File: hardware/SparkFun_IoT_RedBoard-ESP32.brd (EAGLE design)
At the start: 68.6 x 58.4 mm, 215 parts, among them J1 5.5x2.1mm Barrel, J13 QWIIC_RIGHT_ANGLE, J15 MICRO-SD-PUSH-PUSH-EXT-PIN, J2 USB C, J3 USB_SOLDER_PADS, J5 M10NO_SILK, Q1 MBT3904DW1T1, Q11 20V/4.2A/52mΩ/1.4W, Q13 20V/4.2A/52mΩ/1.4W, Q3 20V/4.2A/52mΩ/1.4W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

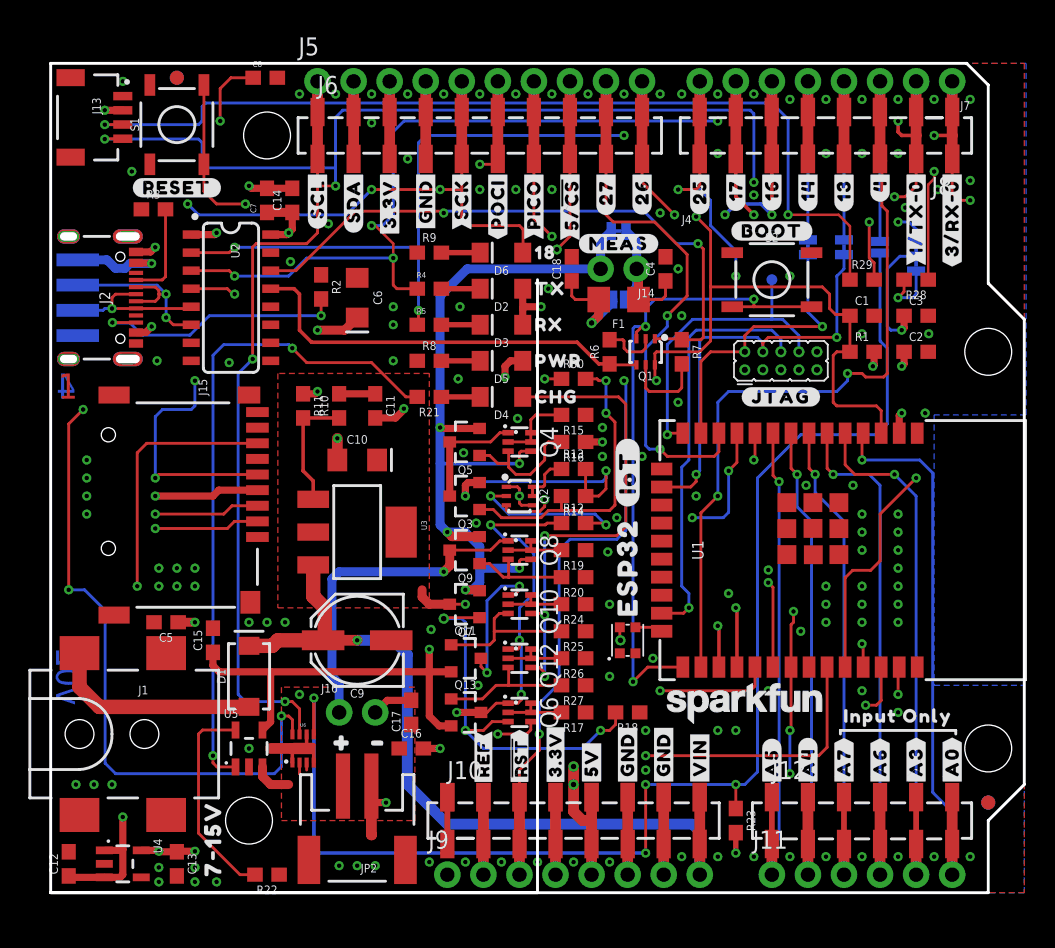
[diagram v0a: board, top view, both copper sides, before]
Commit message: Design review updates
Rename files to remove "v01"
Update libraries
Adjust traces under SD card for keepout region
Change ESP32 footprint from narrow to standard
Change USB-C connector to 4-layer version
Add USB shield jumper
Move CC resistor positions
Adjust parts to be on grid where possible
Move Qwiic logo to top silk (also adjust Reset silk to avoid confusion)
Adjust layer numbers in copper to not overlap
Remove C14
Increase current rating of D1
Add silk to addressable LED
Remove extraneous mill lines
Remove Made in USA silk
Replace MEAS header and jumper with combo jumper
Add fuse value to schematic
Remove voltage ratings from capacitors in schematic
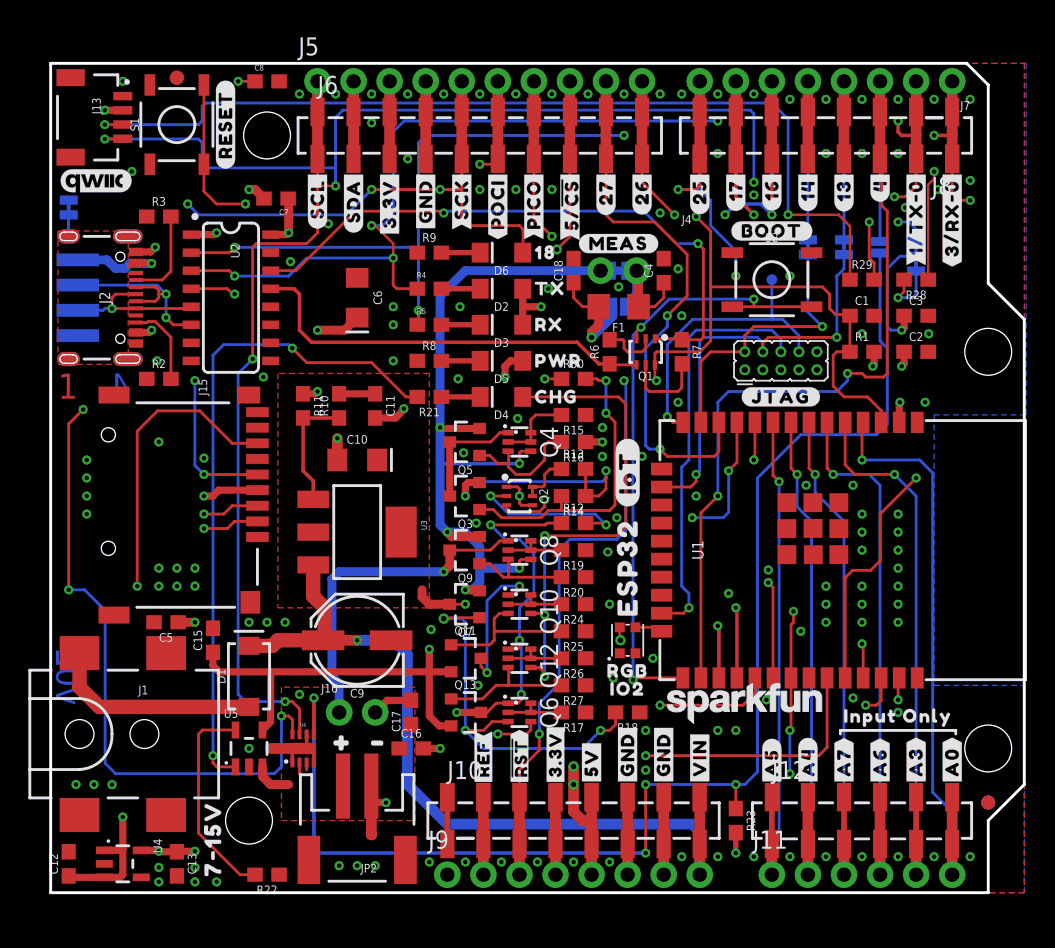
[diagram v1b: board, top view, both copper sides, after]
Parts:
- removed C14: 10uF, SparkFun-Capacitors:0603
- removed J14: (no value), SparkFun-Connectors:1X02_NO_SILK
- removed U$94: (no value), output-ESP32:MADE_IN32321857
- removed U$99: (no value), output-ESP32:THE_USA32321858
- added JP15: SHLD, SparkFun-Jumpers:SMT-JUMPER_2_NC_TRACE_SILK
- added U$65: (no value), output:RGB0
- added U$81: (no value), output:#SHLD#0
- added U$82: (no value), output:IO20
- D1: value 1A/40V/500mV -> 3A/40V/500mV
- F1: value 6V/0.75A -> 6V/0.75A/1.5A
- J2: value USB C -> USB-C; device SparkFun-Connectors:USB-C-16P-2LAYER-PADS -> SparkFun-Connectors:USB-C-16P-4LAYER-ISOLATED
- JP10: value JUMPER-SMT_2_NC_TRACE_SILK -> JUMPER-COMBO_2_NC_TRACE; device SparkFun-Jumpers:SMT-JUMPER_2_NC_TRACE_SILK -> SparkFun-Jumpers:COMBO-JUMPER_2_NC_TRACE
- U$11: device output:#MEAS#0 -> output-ESP32:#MEAS#1851
- U1: value ESP-WROOM-3232D-NARROW -> ESP-WROOM-3232D; device SparkFun-RF:ESP-WROOM-32D-NARROW -> SparkFun-RF:ESP-WROOM-32D
- moved R2 13.1 mm to (7.62, 36.2), turned to 0 degrees
- moved U$11 6.41 mm to (40.0, 45.7)
- moved U$26 5.61 mm to (12.3, 54.1), turned to 90 degrees
- moved LOGO2 4.74 mm to (3.17, 50.2), flipped to the top, turned to 0 degrees
- moved JP10 2.79 mm to (40.0, 43.8)
- moved C7 0.65 mm to (15.9, 48.9), turned to 180 degrees
- moved R3 0.64 mm to (7.62, 47.6)
- moved BYP 0.51 mm to (40.0, 41.3)
- moved F1 0.51 mm to (40.0, 41.3)
- moved U$64 0.51 mm to (45.1, 41.3)
- moved C8 0.28 mm to (15.2, 57.1)
- moved C4 0.18 mm to (43.2, 43.8)
- moved C18 0.18 mm to (36.8, 43.8)
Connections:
- new net SHLD: J2.SHLD1, J2.SHLD2, J2.SHLD3, J2.SHLD4, J2.SHLD5, J2.SHLD6, J2.SHLD7, J2.SHLD8, JP15.2
- net 3.3V: no longer C14.1
- net 5V_MEAS: now also JP10.3; no longer J14.2
- net GND: now also JP15.1, U1.GND; no longer C14.2, U1.GND1
- net N$19: now also JP10.4; no longer J14.1
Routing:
- net CC2: track 18.5 -> 5.88 mm, vias 2 -> 0
- net ESP32_GPIO5_!CS!: track 111.4 -> 104.1 mm
- net ESP32_GPIO23_PICO: track 122.6 -> 115.5 mm
- net ESP32_GPIO18_SCK: track 122.5 -> 117.3 mm
- net 3.3V: track 54.2 -> 49.8 mm
- net 5V_MEAS: track 71.1 -> 68.1 mm
- net ESP32_GPIO19_POCI: track 147.5 -> 150.3 mm
- net V_USB: track 118.5 -> 116.0 mm
- net N$19: track 10.8 -> 8.58 mm
- net ESP32_0: track 46.3 -> 44.5 mm
- net GND: track 46.6 -> 44.8 mm, vias 145 -> 148
- net SHLD: track 0.00 -> 1.52 mm
- net ESP32_EN: track 124.2 -> 122.7 mm
- net N$6: track 21.6 -> 20.4 mm
- net ESP32_GPIO12_TDI: track 21.9 -> 20.8 mm
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- added copper zone on layer 1, net SHLD
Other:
- outline, holes or cut-outs redrawn

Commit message: More design review updates
Add center positive silk marker to barrel jack
Fix air wire errors in ULP by connecting with traces
Add SD card detection with NO jumper to GPIO16
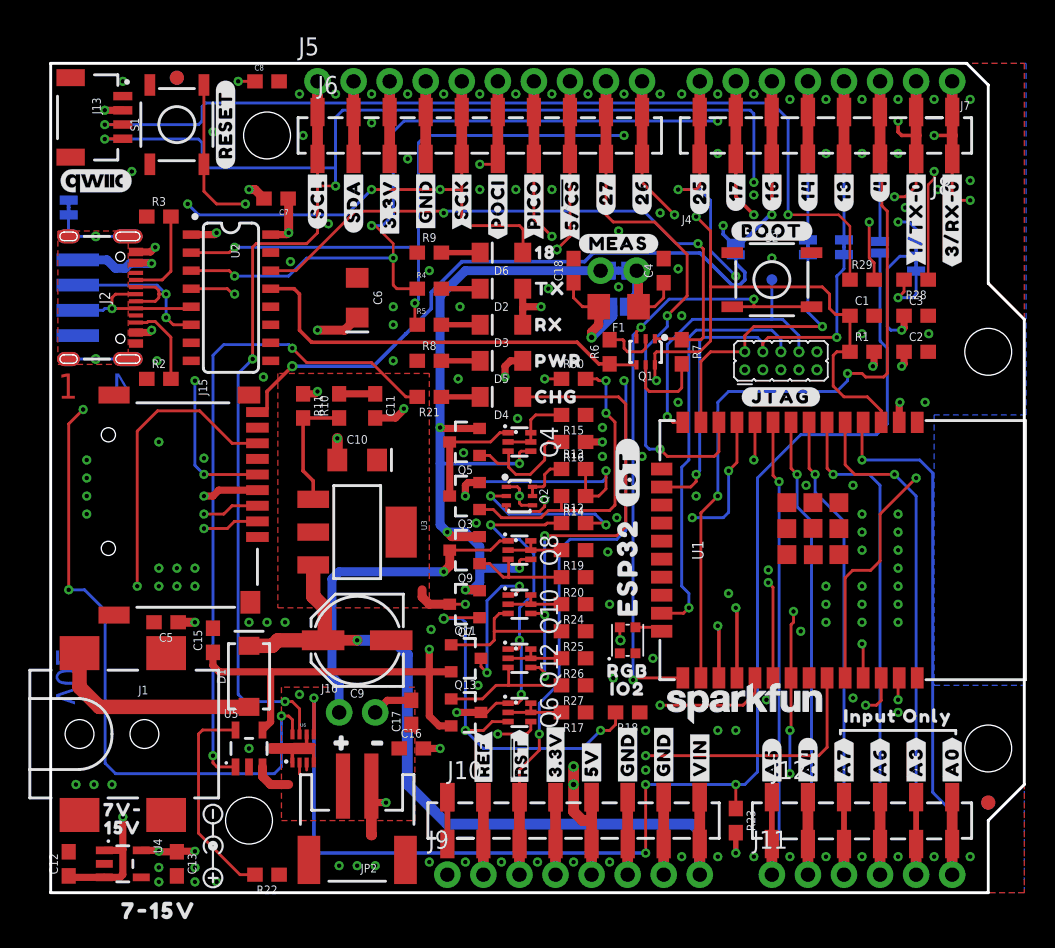
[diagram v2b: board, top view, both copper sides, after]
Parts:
- added JP16: SD_DET, SparkFun-Jumpers:SMT-JUMPER_2_NO_SILK
- added U$106: (no value), output:7V#0
- added U$107: (no value), output:15V0
- added U$108: (no value), output:#SD_DET#0
- added U$94, U$99: (no value), SparkFun-Aesthetics:POLARITY_MARKING_CENTER_POSITIVE#JPG
- moved U$49 6.35 mm to (7.62, -1.27), turned to 0 degrees
- moved U$90 0.13 mm to (58.4, 44.7)
- moved U$89 0.13 mm to (61.0, 43.4)
- moved U$91 0.13 mm to (53.3, 44.6)
- moved U$92 0.13 mm to (55.9, 44.6)
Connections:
- new net N$27: J15.9, JP16.1
- net ESP32_GPIO16: now also JP16.2
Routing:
- net N$27: track 0.00 -> 43.5 mm, vias 0 -> 1
- net SHLD: track 1.52 -> 9.88 mm, vias 0 -> 2
- net N$19: track 8.58 -> 9.35 mm
- net 5V_MEAS: track 68.1 -> 68.9 mm
- net GND: vias 148 -> 152

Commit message: Add NC jumper for each LED
Also fix barrel jack voltage silk
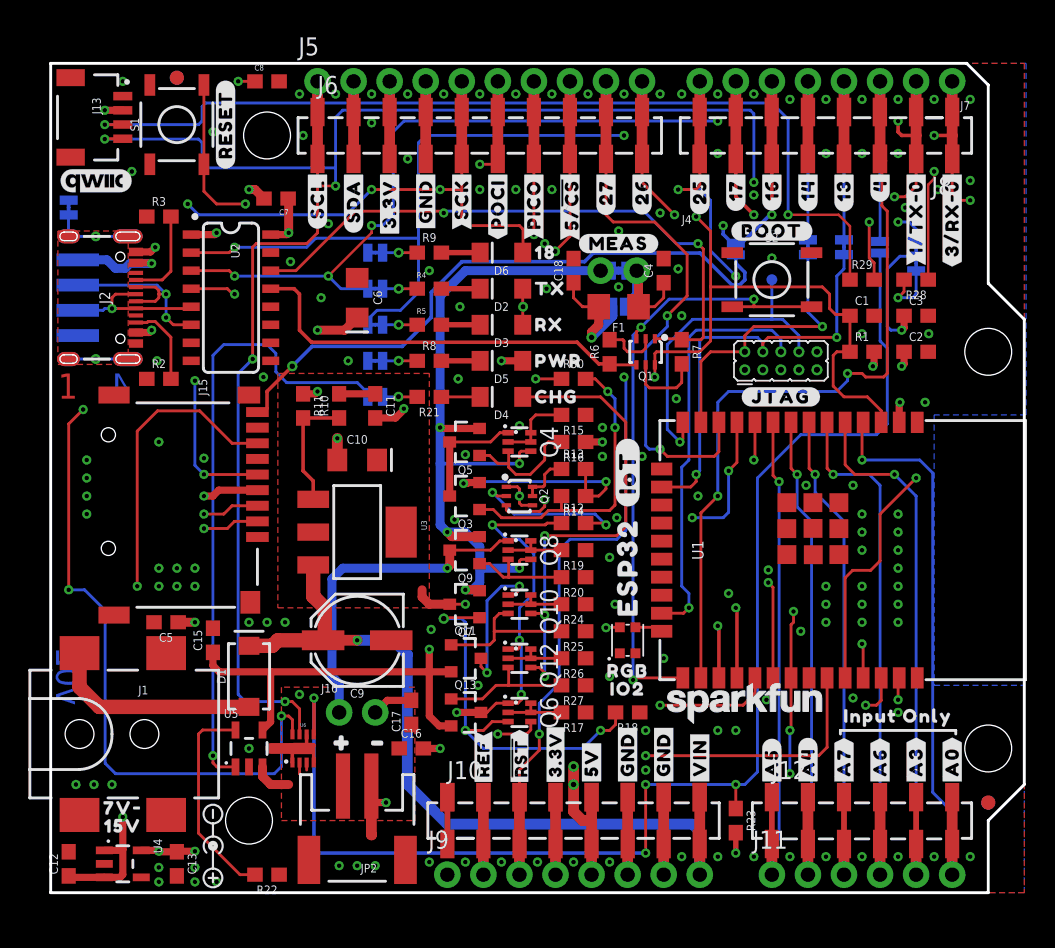
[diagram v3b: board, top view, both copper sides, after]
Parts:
- added JP17, JP18, JP19, JP20, JP21: JUMPER-SMT_2_NC_TRACE_SILK, SparkFun-Jumpers:SMT-JUMPER_2_NC_TRACE_SILK
- added U$109: (no value), output:#LED_TX#0
- added U$110: (no value), output:#LED_RX#0
- added U$111: (no value), output:#LED_PWR#0
- added U$112: (no value), output:#LED_CHG#0
- U$49: device output-ESP32:7#15V32321861 -> output:#LED_18#0
- moved U$49 48.5 mm to (22.0, 45.1), flipped to the bottom
- moved LOGO6 4.02 mm to (35.6, 34.3)
- moved U$103 1.80 mm to (35.6, 17.3)
- moved U$47 1.80 mm to (27.4, 31.4)
- moved U$98 1.80 mm to (47.0, 21.6)
- moved U$93 1.80 mm to (41.3, 20.2)
- moved U$106 0.13 mm to (5.08, 5.97)
- moved U$107 0.13 mm to (5.08, 4.70)
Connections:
- new net N$30: JP20.2, R4.1
- new net N$31: JP19.2, R5.1
- new net N$33: JP18.2, R8.1
- new net N$34: JP21.2, R9.1
- new net N$4: JP17.1, R21.2
- net ESP32_RXD0: now also JP19.1; no longer R5.1
- net ESP32_TXD0: now also JP20.1; no longer R4.1
- net GND: now also JP18.1, JP21.1; no longer R8.1, R9.1
- net N$1: now also JP17.2; no longer R21.2
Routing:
- net ESP32_TXD0: track 111.5 -> 107.6 mm
- net V_USB: track 116.0 -> 113.1 mm
- net N$1: track 46.6 -> 44.1 mm, vias 2 -> 1
- net ESP32_RXD0: track 116.1 -> 118.7 mm, vias 6 -> 5
- net N$4: track 0.00 -> 2.45 mm, vias 0 -> 1
- net N$34: track 0.00 -> 2.44 mm, vias 0 -> 1
- net N$33: track 0.00 -> 2.44 mm, vias 0 -> 1
- net N$31: track 0.00 -> 2.44 mm, vias 0 -> 1
- net N$30: track 0.00 -> 2.44 mm, vias 0 -> 1
- net ESP32_GPIO12_TDI: track 20.8 -> 23.1 mm
- net 3.3V: track 49.8 -> 47.9 mm
- net N$11: track 13.4 -> 14.3 mm
- net 5V_CHG: track 72.1 -> 71.3 mm
- net N$24: track 6.06 -> 5.48 mm
- net ESP32_GPIO23_PICO: track 115.5 -> 114.9 mm

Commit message: Checklist update
Approve DRC errors on jumpers
Add space between traces on layer 2
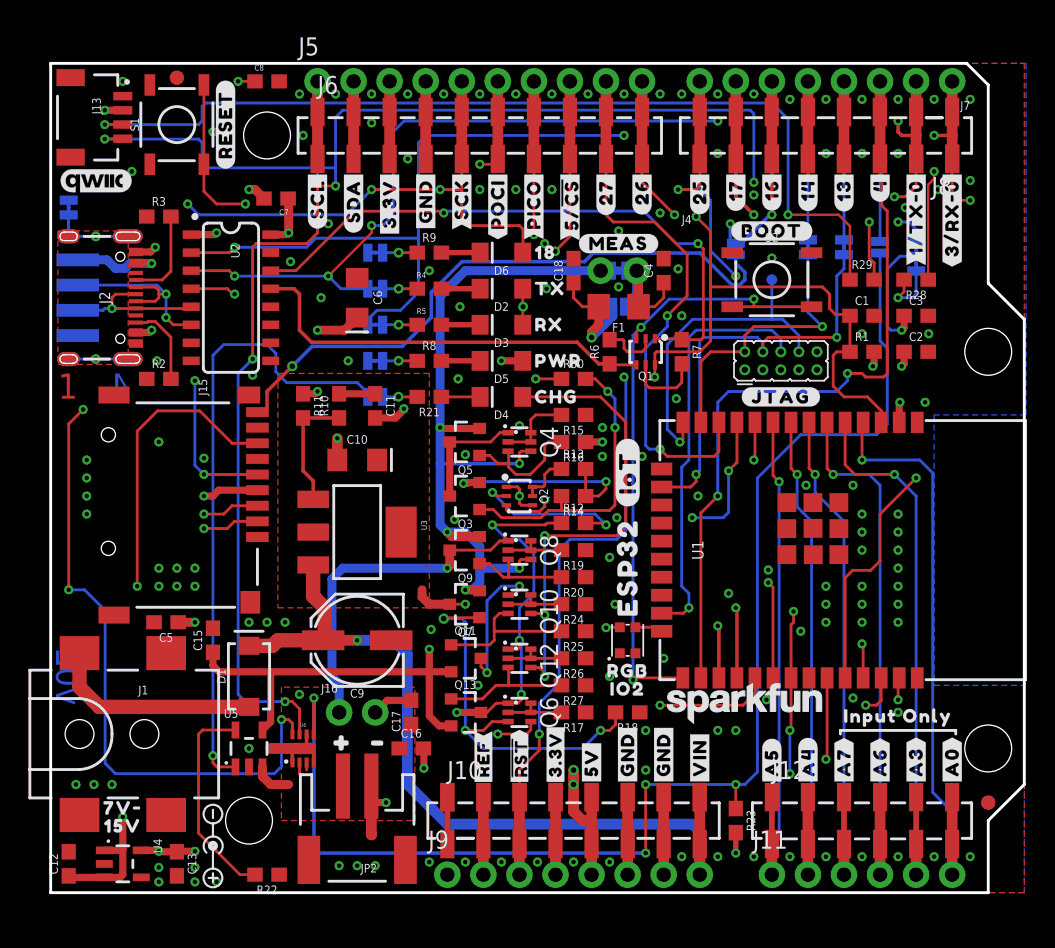
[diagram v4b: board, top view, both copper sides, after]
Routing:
- net ESP32_SCL: track 183.9 -> 182.7 mm
- net ESP32_GPIO25: track 35.0 -> 33.9 mm
- net ESP32_SDA: track 194.2 -> 193.2 mm
- net ESP32_GPIO18_SCK: track 117.3 -> 116.8 mm

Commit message: Design review updates
Change IO2 to GPIO2 in top silk
Remove via restrict regions
Remove test point silk
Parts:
- removed U$82: (no value), output:IO20
- removed U$95: (no value), output-ESP32:TP1321868
- added U$113: (no value), output:GPIO20
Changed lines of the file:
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@@
 <wire x1="66.04" y1="56.896" x2="66.04" y2="42.926" width="0.2032" layer="20"/>
 <text x="0" y="-0.0635" size="0.0254" layer="214" font="vector">D:/SmartProjects/Snc/a4_bn_logo2.bmp</text>
-<rectangle x1="0.635" y1="22.352" x2="2.032" y2="30.607" layer="43"/>
-<rectangle x1="5.715" y1="23.114" x2="7.366" y2="30.607" layer="43"/>
-<rectangle x1="47.879" y1="10.795" x2="48.514" y2="11.303" layer="43"/>
-<rectangle x1="50.419" y1="10.668" x2="50.927" y2="11.557" layer="43"/>
-<rectangle x1="11.303" y1="29.337" x2="12.7" y2="31.623" layer="43"/>
-<rectangle x1="0.254" y1="12.954" x2="9.398" y2="25.019" layer="43"/>
 <rectangle x1="62.484" y1="14.986" x2="68.58" y2="33.274" layer="42"/>
 <text x="51.181" y="-41.148" size="1.778" layer="51">Ricardo Ramos</text>
@@
 <element name="U$97" library="output-ESP32" package="INPUT_ONLY321867" value="" x="59.69" y="10.922" smashed="yes" rot="MR0"/>
 <element name="TP1" library="SparkFun-Connectors" package="PAD.03X.03" value="TEST-POINT3" x="50.8" y="43.18" smashed="yes" rot="MR0"/>
-<element name="U$95" library="output-ESP32" package="TP1321868" value="" x="50.8" y="45.212" smashed="yes" rot="MR90"/>
 <element name="U$98" library="SparkFun-Aesthetics" package="REDBOARD_LOGO" value="" x="46.99" y="21.59" smashed="yes" rot="MR0"/>
 <element name="U$100" library="output-ESP32" package="#IOT#132321869" value="" x="40.64" y="29.591" smashed="yes" rot="R90"/>
@@
 </element>
 <element name="U$65" library="output" package="RGB0" value="" x="40.64" y="15.621" smashed="yes"/>
-<element name="U$82" library="output" package="IO20" value="" x="40.64" y="14.351" smashed="yes"/>
 <element name="U$11" library="output-ESP32" package="#MEAS#1851" value="" x="40.005" y="45.72" smashed="yes" rot="MR0"/>
 <element name="U$94" library="SparkFun-Aesthetics" package="POLARITY_MARKING_CENTER_POSITIVE#JPG" value="" x="11.43" y="3.302" smashed="yes" rot="R270"/>
@@
 <element name="U$111" library="output" package="#LED_PWR#0" value="" x="21.971" y="37.465" smashed="yes" rot="MR0"/>
 <element name="U$112" library="output" package="#LED_CHG#0" value="" x="21.971" y="34.925" smashed="yes" rot="MR0"/>
+<element name="U$113" library="output" package="GPIO20" value="" x="40.64" y="14.351" smashed="yes"/>
 </elements>
 <signals>

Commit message: Fix A4 and A5 bottom silk labels
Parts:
- U$52: device output-ESP32:#34#A6#32321865 -> output:#33#A5#0
- moved U$52 2.54 mm to (50.8, 1.78)
- moved U$54 2.54 mm to (53.3, 1.78)
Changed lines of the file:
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@@
 <element name="U$50" library="output-ESP32" package="#39#A3#321862" value="" x="60.96" y="1.778" smashed="yes" rot="MR90"/>
 <element name="U$51" library="output-ESP32" package="#36#A0#321862" value="" x="63.5" y="1.778" smashed="yes" rot="MR90"/>
-<element name="U$52" library="output-ESP32" package="#34#A6#32321865" value="" x="53.34" y="1.778" smashed="yes" rot="MR90"/>
 <element name="U$53" library="output-ESP32" package="#35#A7#321862" value="" x="55.88" y="1.778" smashed="yes" rot="MR90"/>
-<element name="U$54" library="output-ESP32" package="#32#A4#32321865" value="" x="50.8" y="1.778" smashed="yes" rot="MR90"/>
+<element name="U$54" library="output-ESP32" package="#32#A4#32321865" value="" x="53.34" y="1.778" smashed="yes" rot="MR90"/>
 <element name="U$55" library="output-ESP32" package="#34#A6#321862" value="" x="58.42" y="1.778" smashed="yes" rot="MR90"/>
 <element name="U$56" library="output-ESP32" package="#VIN#321862" value="" x="45.72" y="1.778" smashed="yes" rot="MR90"/>
@@
 <element name="U$112" library="output" package="#LED_CHG#0" value="" x="21.971" y="34.925" smashed="yes" rot="MR0"/>
 <element name="U$113" library="output" package="GPIO20" value="" x="40.64" y="14.351" smashed="yes"/>
+<element name="U$52" library="output" package="#33#A5#0" value="" x="50.8" y="1.778" smashed="yes" rot="MR90"/>
 </elements>
 <signals>

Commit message: Update version number to v10
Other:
- board text added: "v10"
- board text removed: "v02"
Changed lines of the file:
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@@
 <wire x1="55.626" y1="11.43" x2="63.754" y2="11.43" width="0.2032" layer="21"/>
 <wire x1="63.754" y1="11.43" x2="63.754" y2="11.176" width="0.2032" layer="21"/>
-<text x="1.27" y="15.24" size="1.778" layer="16" font="vector" ratio="15" rot="MR270" align="center">v02</text>
+<text x="1.27" y="15.24" size="1.778" layer="16" font="vector" ratio="15" rot="MR270" align="center">v10</text>
 <text x="78.74" y="43.18" size="1.778" layer="51" font="vector" ratio="10">- Board thickness is 1.6mm</text>
 <text x="78.74" y="38.1" size="1.778" layer="51" font="vector" ratio="10">- No clean process</text>
